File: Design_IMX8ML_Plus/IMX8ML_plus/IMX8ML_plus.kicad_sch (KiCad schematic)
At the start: 2 parts, among them U5 MT25QUxxxxxx1xW7, U6 IMX6ModuleConector_300

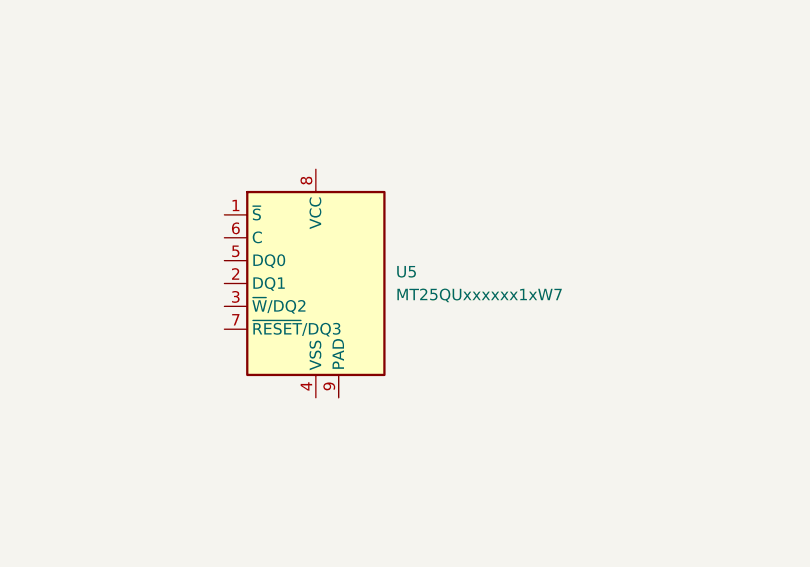
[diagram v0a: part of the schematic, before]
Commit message: Add storage unit
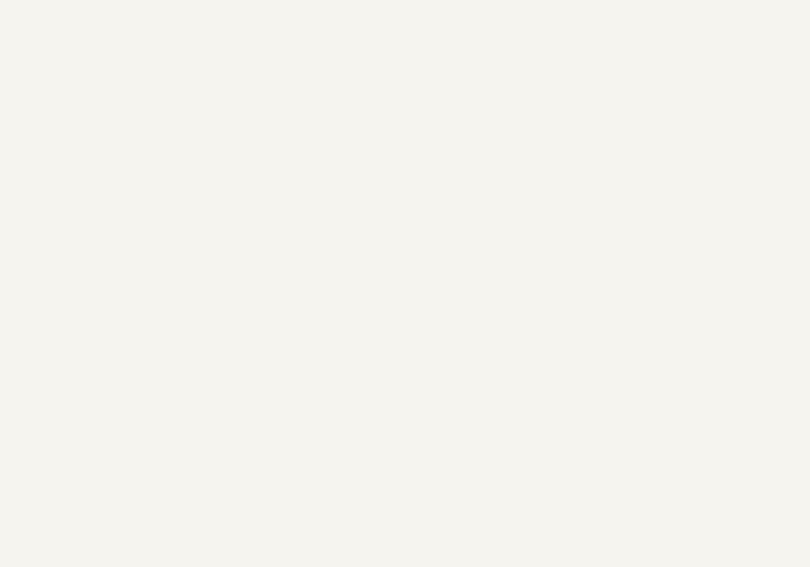
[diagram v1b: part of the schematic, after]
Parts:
- removed U5: MT25QUxxxxxx1xW7, Package_DFN_QFN:W-PDFN-8-1EP_6x5mm_P1.27mm_EP3x3mm, symbol Memory_Flash:MT25QUxxxxxx1xW7
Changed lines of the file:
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@@
 (kicad_sch (version 20230121) (generator eeschema)
   (paper "A4")
-  (symbol (lib_id "Memory_Flash:MT25QUxxxxxx1xW7") (at 118.11 140.97 0) (unit 1)
-    (in_bom yes) (on_board yes) (dnp no) (fields_autoplaced)
-    (property "Reference" "U5" (at 127 139.7 0)
-      (effects (font (size 1.27 1.27)) (justify left))
-    )
-    (property "Value" "MT25QUxxxxxx1xW7" (at 127 142.24 0)
-      (effects (font (size 1.27 1.27)) (justify left))
-    )
-    (property "Footprint" "Package_DFN_QFN:W-PDFN-8-1EP_6x5mm_P1.27mm_EP3x3mm" (at 138.43 138.43 0)
-      (effects (font (size 1.27 1.27)) hide)
-    )
-    (property "Datasheet" "https://media-www.micron.com/-/media/client/global/documents/products/data-sheet/nor-flash/serial-nor/mt25q/die-rev-a/mt25q_qljs_u_256_aba_0.pdf" (at 118.11 123.19 0)
-      (effects (font (size 1.27 1.27)) hide)
-    )
-    (pin "1")
-    (pin "2")
-    (pin "3")
-    (pin "4")
-    (pin "5")
-    (pin "6")
-    (pin "7")
-    (pin "8")
-    (pin "9")
-    (instances
-      (project "IMX8ML_plus"
-        (path "/1e0dca60-79b3-4b5b-ab8f-7b2adbc68a5f/0f9447d4-7a95-466a-adb7-639b0294b239"
-          (reference "U5") (unit 1)
-        )
-        (path "/1e0dca60-79b3-4b5b-ab8f-7b2adbc68a5f"
-          (reference "U5") (unit 1)
-        )
-      )
-    )
-  )
   (symbol (lib_id "_W_MX8M:IMX6ModuleConector_300-William_IMX6QP") (at 228.6 15.24 0) (unit 2)
     (in_bom yes) (on_board yes) (dnp no) (fields_autoplaced)

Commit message: processor capacitors location
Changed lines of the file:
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@@
+    (stroke (width 0) (type default))
+  )
+  (wire (pts (xy 283.21 229.87) (xy 274.32 229.87))
     (stroke (width 0) (type default))
   )
@@
     (stroke (width 0) (type default))
   )
+  (wire (pts (xy 271.78 271.78) (xy 262.89 271.78))
+    (stroke (width 0) (type default))
+  )
   (wire (pts (xy 328.93 95.25) (xy 320.04 95.25))
     (stroke (width 0) (type default))
@@
     (stroke (width 0) (type default))
   )
+  (wire (pts (xy 283.21 237.49) (xy 274.32 237.49))
+    (stroke (width 0) (type default))
+  )
   (wire (pts (xy 407.67 212.09) (xy 398.78 212.09))
     (stroke (width 0) (type default))
@@
     (stroke (width 0) (type default))
   )
+  (wire (pts (xy 283.21 227.33) (xy 274.32 227.33))
+    (stroke (width 0) (type default))
+  )
   (wire (pts (xy 241.3 231.14) (xy 232.41 231.14))
     (stroke (width 0) (type default))
@@
     (stroke (width 0) (type default))
   )
+  (wire (pts (xy 271.78 261.62) (xy 262.89 261.62))
+    (stroke (width 0) (type default))
+  )
   (wire (pts (xy 416.56 109.22) (xy 407.67 109.22))
     (stroke (width 0) (type default))
@@
     (stroke (width 0) (type default))
   )
+  (wire (pts (xy 283.21 224.79) (xy 274.32 224.79))
+    (stroke (width 0) (type default))
+  )
+  (wire (pts (xy 271.78 266.7) (xy 262.89 266.7))
+    (stroke (width 0) (type default))
+  )
   (wire (pts (xy 407.67 229.87) (xy 398.78 229.87))
     (stroke (width 0) (type default))
@@
     (stroke (width 0) (type default))
   )
+  (wire (pts (xy 271.78 264.16) (xy 262.89 264.16))
+    (stroke (width 0) (type default))
+  )
   (wire (pts (xy 429.26 170.18) (xy 420.37 170.18))
     (stroke (width 0) (type default))
@@
     (stroke (width 0) (type default))
   )
+  (wire (pts (xy 271.78 259.08) (xy 262.89 259.08))
+    (stroke (width 0) (type default))
+  )
   (wire (pts (xy 429.26 147.32) (xy 420.37 147.32))
     (stroke (width 0) (type default))
@@
     (stroke (width 0) (type default))
   )
+  (wire (pts (xy 283.21 232.41) (xy 274.32 232.41))
+    (stroke (width 0) (type default))
+  )
   (wire (pts (xy 344.17 58.42) (xy 335.28 58.42))
     (stroke (width 0) (type default))
@@
     (stroke (width 0) (type default))
   )
+  (wire (pts (xy 283.21 240.03) (xy 274.32 240.03))
+    (stroke (width 0) (type default))
+  )
   (wire (pts (xy 429.26 175.26) (xy 420.37 175.26))
     (stroke (width 0) (type default))
@@
     (stroke (width 0) (type default))
   )
+  (wire (pts (xy 283.21 222.25) (xy 274.32 222.25))
+    (stroke (width 0) (type default))
+  )
   (wire (pts (xy 370.84 66.04) (xy 361.95 66.04))
     (stroke (width 0) (type default))
@@
     (stroke (width 0) (type default))
   )
+  (wire (pts (xy 271.78 269.24) (xy 262.89 269.24))
+    (stroke (width 0) (type default))
+  )
   (wire (pts (xy 241.3 223.52) (xy 232.41 223.52))
     (stroke (width 0) (type default))
@@
     (stroke (width 0) (type default))
   )
+  (wire (pts (xy 271.78 274.32) (xy 262.89 274.32))
+    (stroke (width 0) (type default))
+  )
   (wire (pts (xy 358.14 195.58) (xy 349.25 195.58))
     (stroke (width 0) (type default))
@@
     )
   )
+  (global_label "SAI2_TXC" (shape input) (at 274.32 229.87 180) (fields_autoplaced)
+    (effects (font (size 1 1)) (justify right))
+    (property "Intersheetrefs" "${INTERSHEET_REFS}" (at 265.3178 229.87 0)
+      (effects (font (size 1.27 1.27)) (justify right) hide)
+    )
+  )
   (global_label "BOOT_MODE1" (shape input) (at 165.1 29.21 180) (fields_autoplaced)
     (effects (font (size 1 1)) (justify right))
@@
     )
   )
+  (global_label "SAI3_TXD" (shape input) (at 262.89 271.78 180) (fields_autoplaced)
+    (effects (font (size 1 1)) (justify right))
+    (property "Intersheetrefs" "${INTERSHEET_REFS}" (at 253.8878 271.78 0)
+      (effects (font (size 1.27 1.27)) (justify right) hide)
+    )
+  )
   (global_label "SAI1_TXD2" (shape input) (at 398.78 232.41 180) (fields_autoplaced)
     (effects (font (size 1 1)) (justify right))
@@
     )
   )
+  (global_label "SAI3_RXC" (shape input) (at 262.89 261.62 180) (fields_autoplaced)
+    (effects (font (size 1 1)) (justify right))
+    (property "Intersheetrefs" "${INTERSHEET_REFS}" (at 253.6497 261.62 0)
+      (effects (font (size 1.27 1.27)) (justify right) hide)
+    )
+  )
   (global_label "HDM_TX0_P" (shape input) (at 318.77 34.29 180) (fields_autoplaced)
     (effects (font (size 1 1)) (justify right))
@@
     )
   )
+  (global_label "SAI3_TXC" (shape input) (at 262.89 269.24 180) (fields_autoplaced)
+    (effects (font (size 1 1)) (justify right))
+    (property "Intersheetrefs" "${INTERSHEET_REFS}" (at 253.8878 269.24 0)
+      (effects (font (size 1.27 1.27)) (justify right) hide)
+    )
+  )
+  (global_label "SAI3_TXFS" (shape input) (at 262.89 274.32 180) (fields_autoplaced)
+    (effects (font (size 1 1)) (justify right))
+    (property "Intersheetrefs" "${INTERSHEET_REFS}" (at 253.0783 274.32 0)
+      (effects (font (size 1.27 1.27)) (justify right) hide)
+    )
+  )
   (global_label "UART3_TXD" (shape input) (at 407.67 116.84 180) (fields_autoplaced)
     (effects (font (size 1 1)) (justify right))
@@
     )
   )
+  (global_label "SAI3_RXD" (shape input) (at 262.89 264.16 180) (fields_autoplaced)
+    (effects (font (size 1 1)) (justify right))
+    (property "Intersheetrefs" "${INTERSHEET_REFS}" (at 253.6497 264.16 0)
+      (effects (font (size 1.27 1.27)) (justify right) hide)
+    )
+  )
   (global_label "GPIO1_IO08" (shape input) (at 420.37 162.56 180) (fields_autoplaced)
     (effects (font (size 1 1)) (justify right))
@@
     )
   )
+  (global_label "SAI2_RXC" (shape input) (at 274.32 224.79 180) (fields_autoplaced)
+    (effects (font (size 1 1)) (justify right))
+    (property "Intersheetrefs" "${INTERSHEET_REFS}" (at 265.0797 224.79 0)
+      (effects (font (size 1.27 1.27)) (justify right) hide)
+    )
+  )
+  (global_label "SAI3_MCLK" (shape input) (at 262.89 259.08 180) (fields_autoplaced)
+    (effects (font (size 1 1)) (justify right))
+    (property "Intersheetrefs" "${INTERSHEET_REFS}" (at 252.6497 259.08 0)
+      (effects (font (size 1.27 1.27)) (justify right) hide)
+    )
+  )
   (global_label "LVDS1_CLK_P" (shape input) (at 328.93 246.38 180) (fields_autoplaced)
     (effects (font (size 1 1)) (justify right))
@@
     )
   )
+  (global_label "SAI2_MCLK" (shape input) (at 274.32 222.25 180) (fields_autoplaced)
+    (effects (font (size 1 1)) (justify right))
+    (property "Intersheetrefs" "${INTERSHEET_REFS}" (at 264.0797 222.25 0)
+      (effects (font (size 1.27 1.27)) (justify right) hide)
+    )
+  )
   (global_label "SDC1_DATA7" (shape input) (at 415.29 45.72 180) (fields_autoplaced)
     (effects (font (size 1 1)) (justify right))
@@
     )
   )
+  (global_label "SAI2_TXFS" (shape input) (at 274.32 232.41 180) (fields_autoplaced)
+    (effects (font (size 1 1)) (justify right))
+    (property "Intersheetrefs" "${INTERSHEET_REFS}" (at 264.5083 232.41 0)
+      (effects (font (size 1.27 1.27)) (justify right) hide)
+    )
+  )
   (global_label "GPIO1_IO05" (shape input) (at 420.37 154.94 180) (fields_autoplaced)
     (effects (font (size 1 1)) (justify right))
@@
     )
   )
+  (global_label "SAI2_TXD0" (shape input) (at 274.32 240.03 180) (fields_autoplaced)
+    (effects (font (size 1 1)) (justify right))
+    (property "Intersheetrefs" "${INTERSHEET_REFS}" (at 264.3654 240.03 0)
+      (effects (font (size 1.27 1.27)) (justify right) hide)
+    )
+  )
   (global_label "CLKIN1" (shape input) (at 165.1 38.1 180) (fields_autoplaced)
     (effects (font (size 1 1)) (justify right))
@@
     )
   )
+  (global_label "SAI2_RXFS" (shape input) (at 274.32 227.33 180) (fields_autoplaced)
+    (effects (font (size 1 1)) (justify right))
+    (property "Intersheetrefs" "${INTERSHEET_REFS}" (at 264.2702 227.33 0)
+      (effects (font (size 1.27 1.27)) (justify right) hide)
+    )
+  )
   (global_label "LVDS0_D1_N" (shape input) (at 349.25 195.58 180) (fields_autoplaced)
     (effects (font (size 1 1)) (justify right))
@@
     )
   )
+  (global_label "SAI3_RXFS" (shape input) (at 262.89 266.7 180) (fields_autoplaced)
+    (effects (font (size 1 1)) (justify right))
+    (property "Intersheetrefs" "${INTERSHEET_REFS}" (at 252.8402 266.7 0)
+      (effects (font (size 1.27 1.27)) (justify right) hide)
+    )
+  )
   (global_label "CSI1_D1_N" (shape input) (at 335.28 63.5 180) (fields_autoplaced)
     (effects (font (size 1 1)) (justify right))
@@
       (effects (font (size 1.27 1.27)) (justify right) hide)
     )
+  )
+  (global_label "SAI2_RXD0" (shape input) (at 274.32 237.49 180) (fields_autoplaced)
+    (effects (font (size 1 1)) (justify right))
+    (property "Intersheetrefs" "${INTERSHEET_REFS}" (at 264.1273 237.49 0)
+      (effects (font (size 1.27 1.27)) (justify right) hide)
+    )

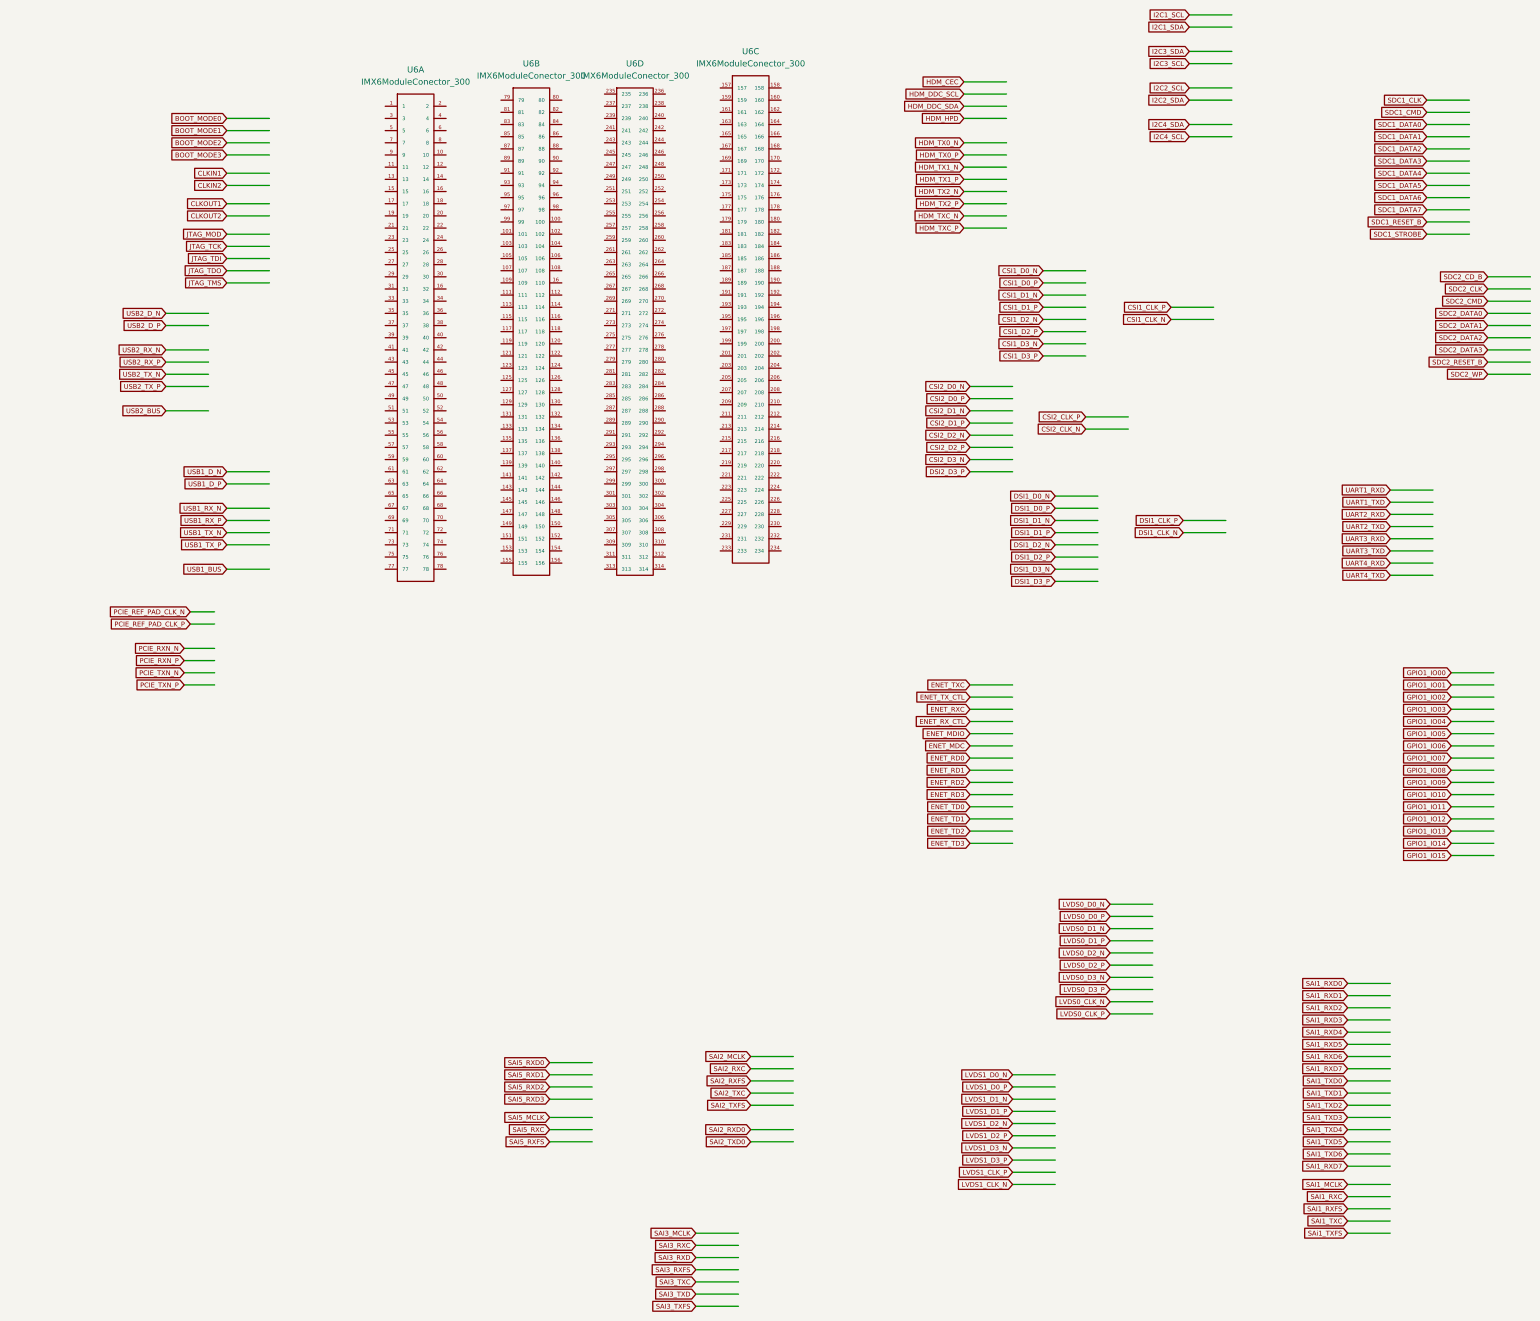
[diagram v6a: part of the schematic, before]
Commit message: Changes the contector for DF40C-100Dx
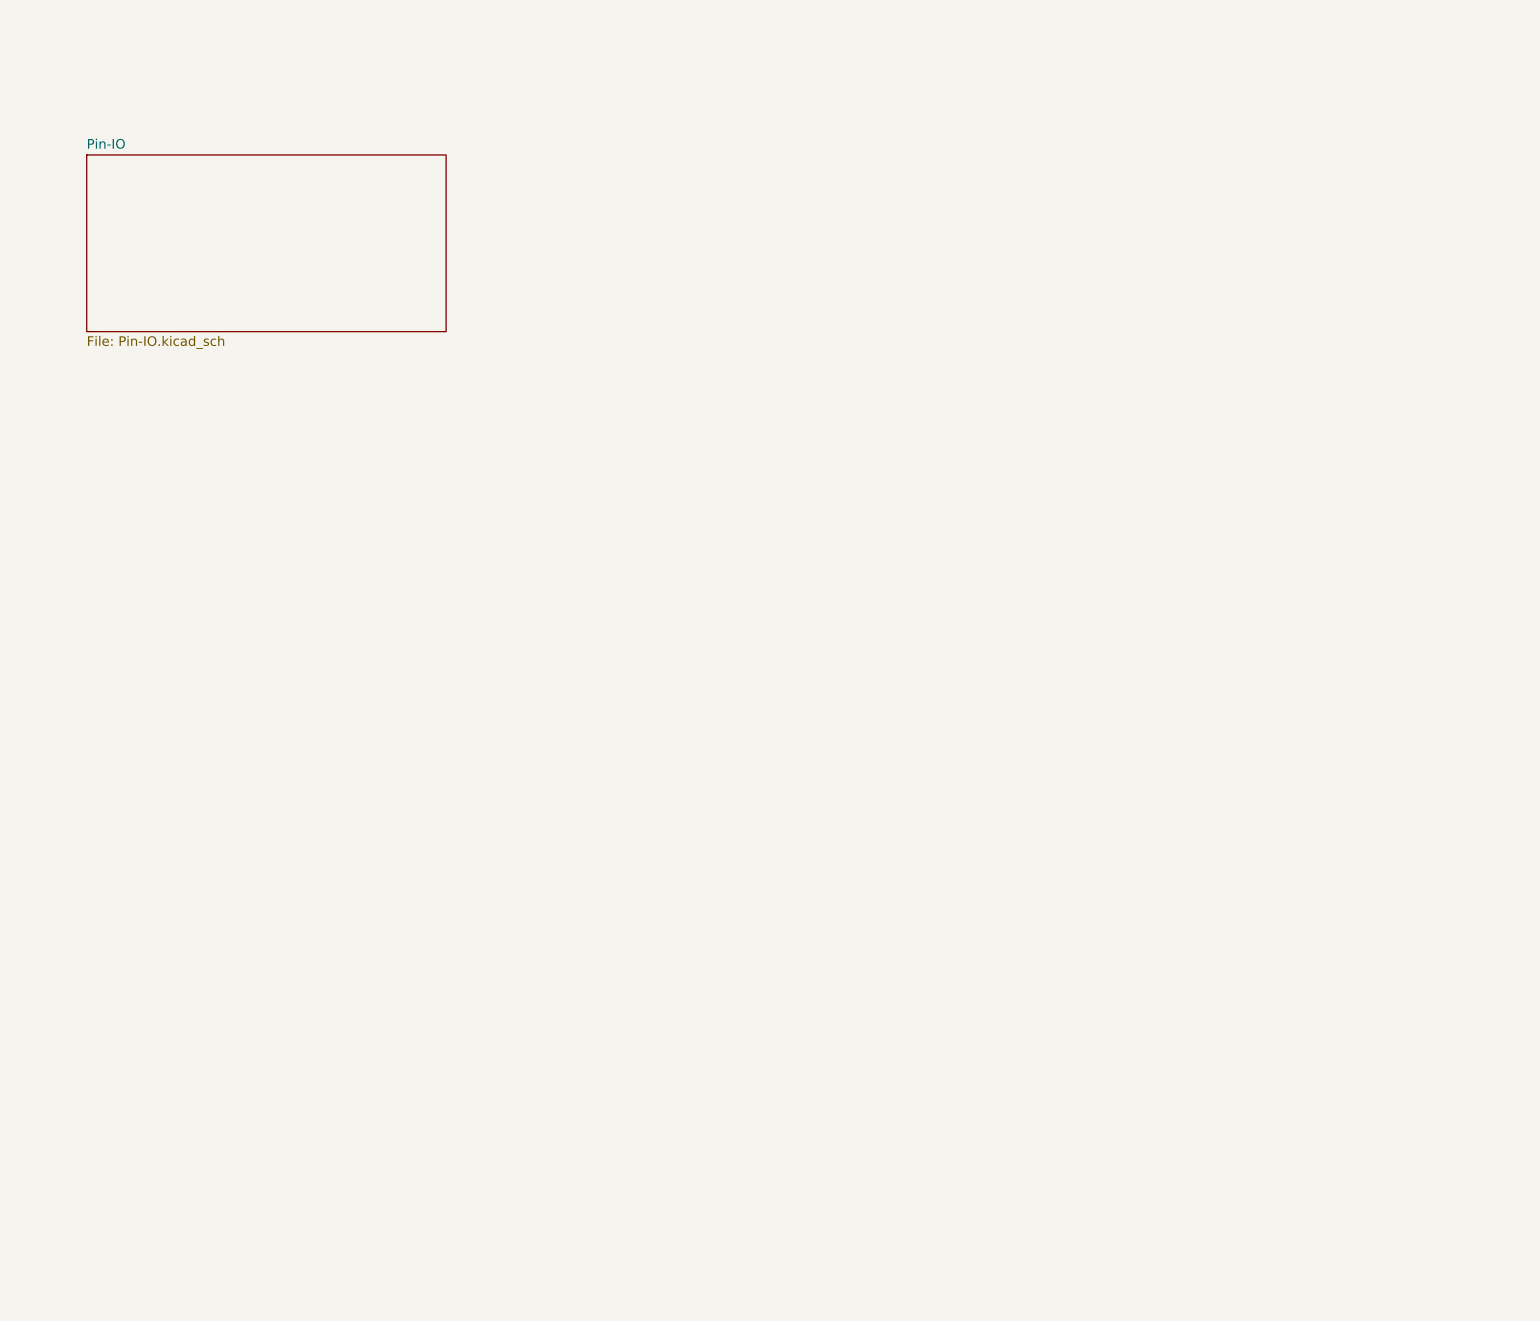
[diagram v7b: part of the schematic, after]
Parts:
- removed U6: IMX6ModuleConector_300, _W_SBC:IMX6QPModule_R300, symbol _W_MX8M:IMX6ModuleConector_300-William_IMX6QP
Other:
- added sheet Pin-IO (Pin-IO.kicad_sch)
